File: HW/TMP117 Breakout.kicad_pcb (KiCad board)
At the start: 2 copper layers, 26.6 x 18.3 mm, 6 parts, among them J1 IO, U1 TMP117xxDRV

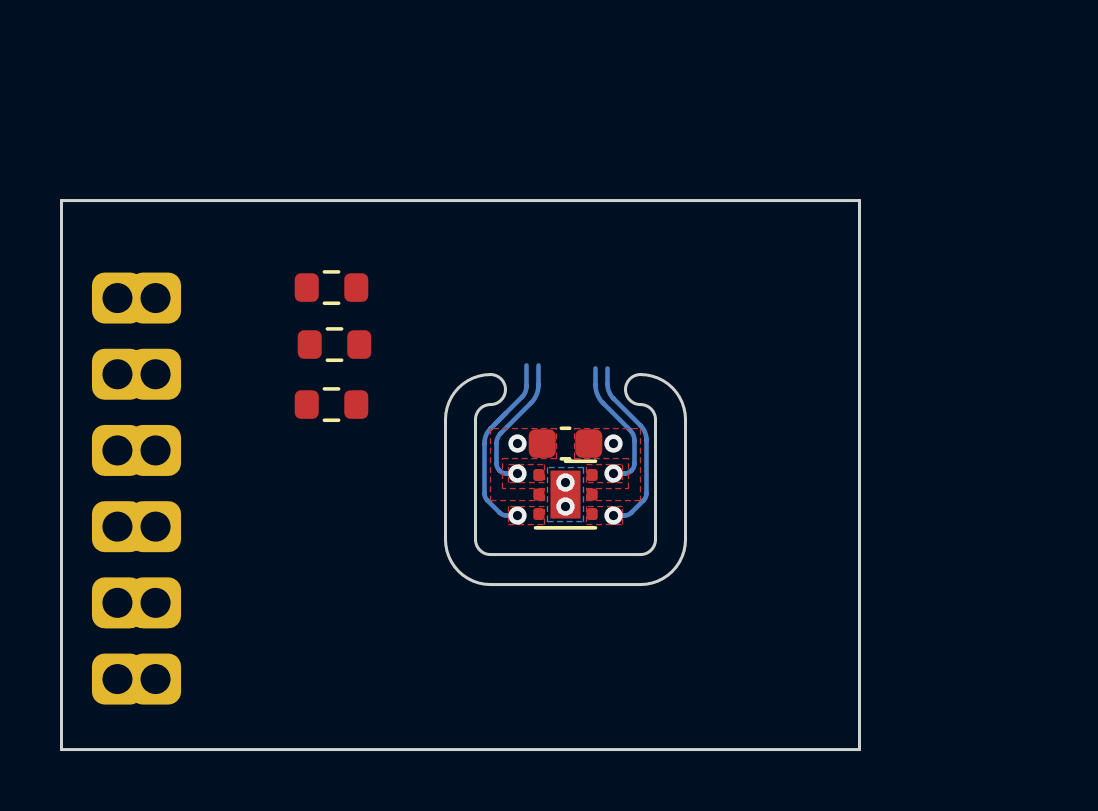
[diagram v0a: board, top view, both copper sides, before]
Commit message: Completed layout
- Completed PCB layout and routing
- Plotted GERBER files
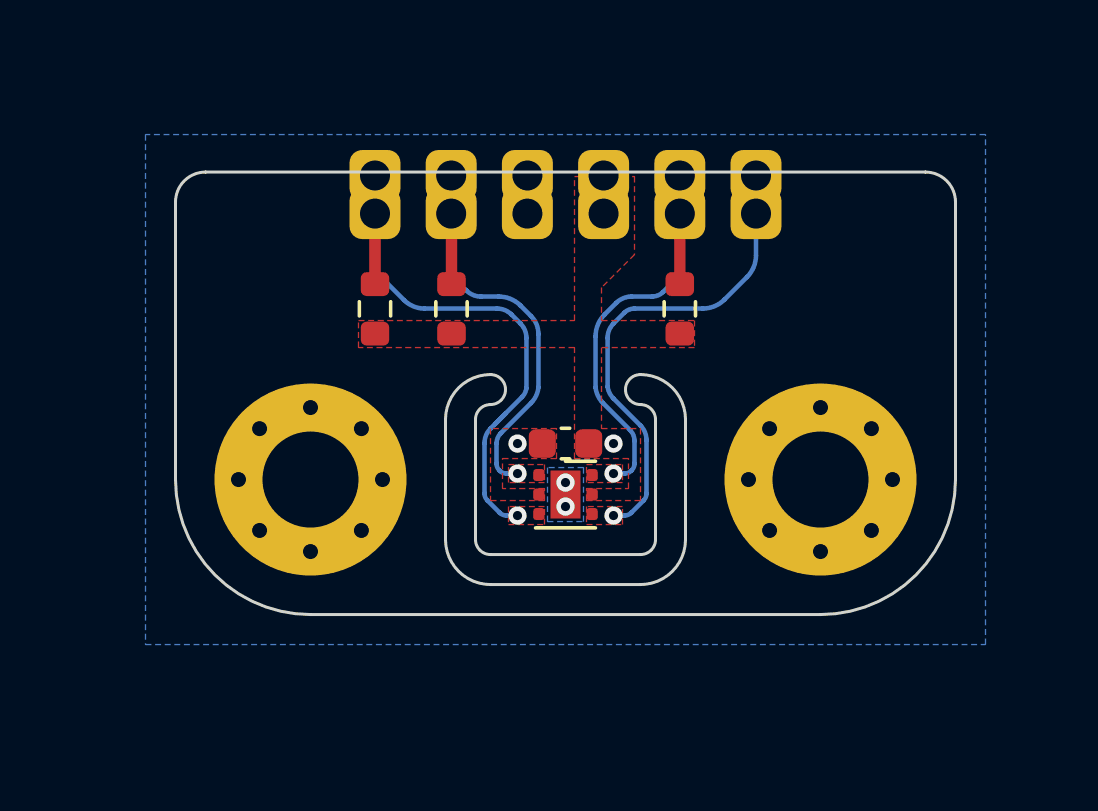
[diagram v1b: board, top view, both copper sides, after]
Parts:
- added H1: MountingHole, MountingHole:MountingHole_3.2mm_M3_Pad_Via, F.Cu at (148.5, 99.5)
- added H2: MountingHole, MountingHole:MountingHole_3.2mm_M3_Pad_Via, F.Cu at (131.5, 99.5)
- moved R1 12.0 mm to (143.8, 93.8), turned to 90 degrees
- moved J1 9.03 mm to (133.7, 90.6), turned to 90 degrees
- moved R2 4.06 mm to (136.2, 93.8), turned to 90 degrees
- moved R3 1.80 mm to (133.7, 93.8), turned to 90 degrees
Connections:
- J1 pad 1: unconnected-(J1-Pin_1-Pad1) -> /ALERT
- J1 pad 2: unconnected-(J1-Pin_2-Pad2) -> /SCL
- J1 pad 3: unconnected-(J1-Pin_3-Pad3) -> GND
- J1 pad 4: unconnected-(J1-Pin_4-Pad4) -> VCC
- J1 pad 5: unconnected-(J1-Pin_5-Pad5) -> /SDA
- J1 pad 6: unconnected-(J1-Pin_6-Pad6) -> /ADD0
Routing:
- net /ALERT: track 6.73 -> 17.9 mm
- net /SDA: track 4.52 -> 13.8 mm
- net /SCL: track 4.67 -> 13.9 mm
- net /ADD0: track 6.09 -> 14.8 mm
- added copper zone on B.Cu, net GND
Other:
- board size 26.6 x 18.3 mm -> 26 x 14.8 mm

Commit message: Updated files
- Added NNNI branding
- Updated traces to regions
- Updated Image
- Reexported GERBER files
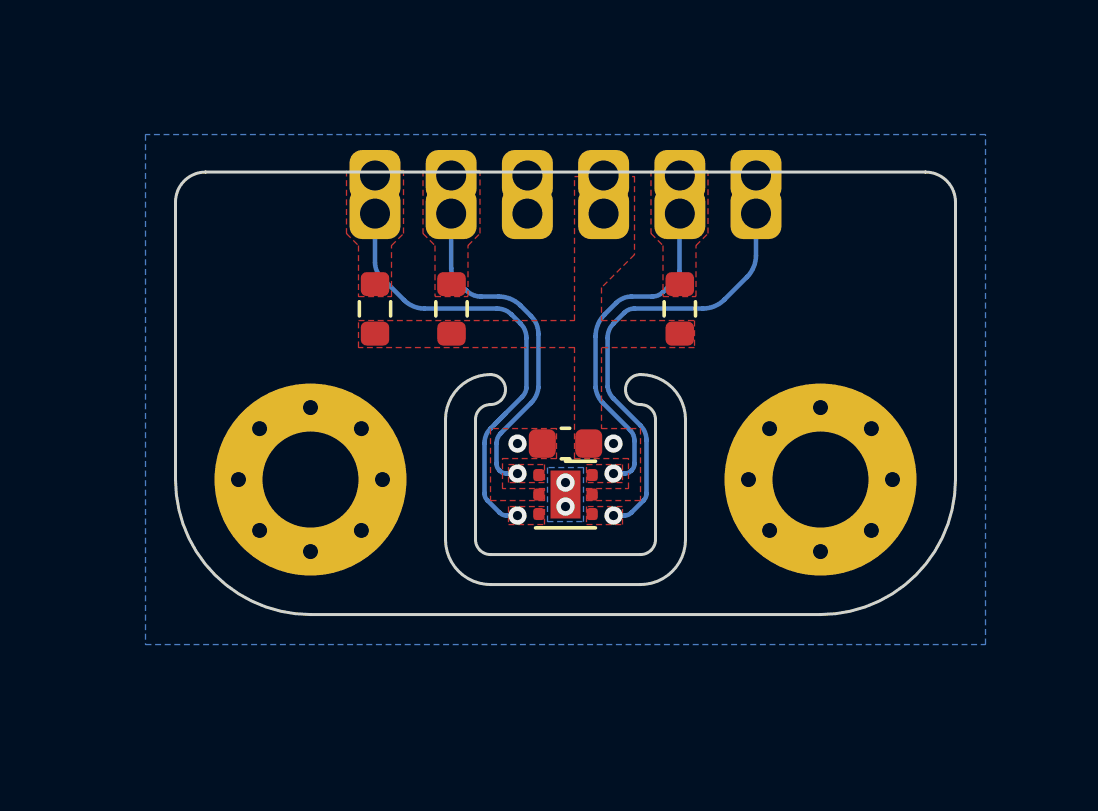
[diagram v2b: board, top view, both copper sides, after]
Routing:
- net /SDA: track 13.8 -> 11.4 mm
- net /ALERT: track 17.9 -> 15.6 mm
- net /SCL: track 13.9 -> 11.6 mm
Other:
- board text added: "TMP117 NNNI 2323"
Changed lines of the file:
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@@
   (gr_arc (start 137 97.5) (mid 137.146447 97.146447) (end 137.5 97)
     (stroke (width 0.1) (type default)) (layer "Edge.Cuts"))
+  (gr_text "TMP117\nNNNI 2323" (at 152.25 90 90) (layer "B.Mask")
+    (effects (font (size 0.8128 0.8128) (thickness 0.1524) bold) (justify left bottom mirror))
+  )
   (via (at 138.4 98.3) (size 0.6096) (drill 0.3048) (layers "F.Cu" "B.Cu") (free) (net 1))
-  (segment (start 136.2 92.985) (end 136.2 90.645) (width 0.381) (layer "F.Cu") (net 2))
   (segment (start 136.2 90.645) (end 136.19 90.635) (width 0.381) (layer "F.Cu") (net 2))
   (via (at 138.4 99.3) (size 0.6096) (drill 0.3048) (layers "F.Cu" "B.Cu") (free) (net 2))
@@
   (arc (start 136.7 93.2) (mid 136.921529 93.348022) (end 137.182842 93.4) (width 0.1524) (layer "B.Cu") (net 2))
   (arc (start 137.7 98.958579) (mid 137.72599 99.089236) (end 137.8 99.2) (width 0.1524) (layer "B.Cu") (net 2))
-  (segment (start 133.65 92.985) (end 133.65 90.635) (width 0.381) (layer "F.Cu") (net 3))
   (via (at 138.4 100.7) (size 0.6096) (drill 0.3048) (layers "F.Cu" "B.Cu") (free) (net 3))
   (segment (start 138.2 94) (end 138.5 94.3) (width 0.1524) (layer "B.Cu") (net 3))
@@
   (arc (start 146.35 92.025736) (mid 146.272033 92.417704) (end 146.05 92.75) (width 0.1524) (layer "B.Cu") (net 4))
   (arc (start 141.6 94.3) (mid 141.453943 94.518589) (end 141.402655 94.776432) (width 0.1524) (layer "B.Cu") (net 4))
-  (segment (start 143.81 92.985) (end 143.81 90.635) (width 0.381) (layer "F.Cu") (net 5))
   (via (at 141.6 99.3) (size 0.6096) (drill 0.3048) (layers "F.Cu" "B.Cu") (free) (net 5))
   (segment (start 142.3 98.212132) (end 142.3 98.958579) (width 0.1524) (layer "B.Cu") (net 5))
@@
     (connect_pads yes (clearance 0.127))
     (min_thickness 0.127) (filled_areas_thickness no)
-    (fill yes (thermal_gap 0.127) (thermal_bridge_width 0.5) (smoothing fillet) (radius 0.127) (island_removal_mode 1) (island_area_min 9.999998))
+    (fill yes (thermal_gap 0.127) (thermal_bridge_width 0.5) (smoothing fillet) (radius 0.254) (island_removal_mode 1) (island_area_min 9.999997))
     (polygon
       (pts
@@
     )
   )
+  (zone (net 3) (net_name "/ALERT") (layer "F.Cu") (hatch edge 0.5)
+    (priority 6)
+    (connect_pads yes (clearance 0.127))
+    (min_thickness 0.127) (filled_areas_thickness no)
+    (fill yes (thermal_gap 0.127) (thermal_bridge_width 0.5) (smoothing fillet) (radius 0.254) (island_removal_mode 1) (island_area_min 9.999997))
+    (polygon
+      (pts
+        (xy 132.7 89.2)
+        (xy 132.7 91.3)
+        (xy 133.1 91.7)
+        (xy 133.1 93.4)
+        (xy 134.2 93.4)
+        (xy 134.2 91.7)
+        (xy 134.6 91.3)
+        (xy 134.6 89.2)
+      )
+    )
+  )
   (zone (net 6) (net_name "VCC") (layer "F.Cu") (hatch edge 0.5)
     (priority 1)
     (connect_pads yes (clearance 0.127))
     (min_thickness 0.127) (filled_areas_thickness no)
-    (fill yes (thermal_gap 0.127) (thermal_bridge_width 0.5) (smoothing fillet) (radius 0.254) (island_removal_mode 1) (island_area_min 9.999998))
+    (fill yes (thermal_gap 0.127) (thermal_bridge_width 0.5) (smoothing fillet) (radius 0.254) (island_removal_mode 1) (island_area_min 9.999997))
     (polygon
       (pts
@@
     (connect_pads yes (clearance 0.127))
     (min_thickness 0.127) (filled_areas_thickness no)
-    (fill yes (thermal_gap 0.127) (thermal_bridge_width 0.5) (smoothing fillet) (radius 0.254) (island_removal_mode 1) (island_area_min 9.999998))
+    (fill yes (thermal_gap 0.127) (thermal_bridge_width 0.5) (smoothing fillet) (radius 0.254) (island_removal_mode 1) (island_area_min 9.999997))
     (polygon
       (pts
@@
     )
   )
+  (zone (net 5) (net_name "/SDA") (layer "F.Cu") (hatch edge 0.5)
+    (priority 6)
+    (connect_pads yes (clearance 0.127))
+    (min_thickness 0.127) (filled_areas_thickness no)
+    (fill yes (thermal_gap 0.127) (thermal_bridge_width 0.5) (smoothing fillet) (radius 0.254) (island_removal_mode 1) (island_area_min 9.999996))
+    (polygon
+      (pts
+        (xy 142.85 89.2)
+        (xy 142.85 91.3)
+        (xy 143.25 91.7)
+        (xy 143.25 93.4)
+        (xy 144.35 93.4)
+        (xy 144.35 91.7)
+        (xy 144.75 91.3)
+        (xy 144.75 89.2)
+      )
+    )
+  )
   (zone (net 2) (net_name "/SCL") (layer "F.Cu") (hatch edge 0.5)
     (priority 3)
     (connect_pads yes (clearance 0.127))
     (min_thickness 0.127) (filled_areas_thickness no)
-    (fill yes (thermal_gap 0.127) (thermal_bridge_width 0.5) (smoothing fillet) (radius 0.254) (island_removal_mode 1) (island_area_min 9.999998))
+    (fill yes (thermal_gap 0.127) (thermal_bridge_width 0.5) (smoothing fillet) (radius 0.254) (island_removal_mode 1) (island_area_min 9.999997))
     (polygon
       (pts
@@
     )
   )
+  (zone (net 2) (net_name "/SCL") (layer "F.Cu") (hatch edge 0.5)
+    (priority 6)
+    (connect_pads yes (clearance 0.127))
+    (min_thickness 0.127) (filled_areas_thickness no)
+    (fill yes (thermal_gap 0.127) (thermal_bridge_width 0.5) (smoothing fillet) (radius 0.254) (island_removal_mode 1) (island_area_min 9.999996))
+    (polygon
+      (pts
+        (xy 135.25 89.2)
+        (xy 135.25 91.3)
+        (xy 135.65 91.7)
+        (xy 135.65 93.4)
+        (xy 136.75 93.4)
+        (xy 136.75 91.7)
+        (xy 137.15 91.3)
+        (xy 137.15 89.2)
+      )
+    )
+  )
   (zone (net 3) (net_name "/ALERT") (layer "F.Cu") (hatch edge 0.5)
     (priority 4)
     (connect_pads yes (clearance 0.127))
     (min_thickness 0.127) (filled_areas_thickness no)
-    (fill yes (thermal_gap 0.127) (thermal_bridge_width 0.5) (smoothing fillet) (radius 0.254) (island_removal_mode 1) (island_area_min 9.999998))
+    (fill yes (thermal_gap 0.127) (thermal_bridge_width 0.5) (smoothing fillet) (radius 0.254) (island_removal_mode 1) (island_area_min 9.999997))
     (polygon
       (pts
@@
     (connect_pads yes (clearance 0.127))
     (min_thickness 0.127) (filled_areas_thickness no)
-    (fill yes (thermal_gap 0.127) (thermal_bridge_width 0.5) (smoothing fillet) (radius 0.254) (island_removal_mode 1) (island_area_min 9.999998))
+    (fill yes (thermal_gap 0.127) (thermal_bridge_width 0.5) (smoothing fillet) (radius 0.254) (island_removal_mode 1) (island_area_min 9.999997))
     (polygon
       (pts
@@
     (connect_pads yes (clearance 0.127))
     (min_thickness 0.127) (filled_areas_thickness no)
-    (fill yes (thermal_gap 0.127) (thermal_bridge_width 0.5) (smoothing fillet) (radius 0.254) (island_removal_mode 1) (island_area_min 9.999999))
+    (fill yes (thermal_gap 0.127) (thermal_bridge_width 0.5) (smoothing fillet) (radius 0.254) (island_removal_mode 1) (island_area_min 9.999997))
     (polygon
       (pts
@@
     (connect_pads yes (clearance 0.127))
     (min_thickness 0.127) (filled_areas_thickness no)
-    (fill yes (thermal_gap 0.127) (thermal_bridge_width 0.5) (smoothing fillet) (radius 0.254) (island_removal_mode 2) (island_area_min 2.5))
+    (fill yes (thermal_gap 0.127) (thermal_bridge_width 0.5) (smoothing fillet) (radius 0.254) (island_removal_mode 1) (island_area_min 9.999997))
     (polygon
       (pts
@@
     (connect_pads yes (clearance 0.127))
     (min_thickness 0.127) (filled_areas_thickness no)
-    (fill yes (thermal_gap 0.127) (thermal_bridge_width 0.5) (smoothing fillet) (radius 0.254) (island_removal_mode 1) (island_area_min 9.999998))
-    (polygon
-      (pts
+    (fill yes (thermal_gap 0.127) (thermal_bridge_width 0.5) (smoothing fillet) (radius 0.254) (island_removal_mode 1) (island_area_min 9.999997))
+    (polygon
+      (pts

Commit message: Updated files
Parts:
- moved J1 0.38 mm to (133.7, 90.3)
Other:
- board size 26 x 14.8 mm -> 31.4 x 20.1 mm
